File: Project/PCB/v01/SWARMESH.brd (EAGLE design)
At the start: 100 x 80 mm, 45 parts, among them IC1 4051N, M1 MOTOR10MM, M2 MOTOR10MM, Q1 TIP122, U1 ESP32DEVKITC, U3 L293D, U4 7805T

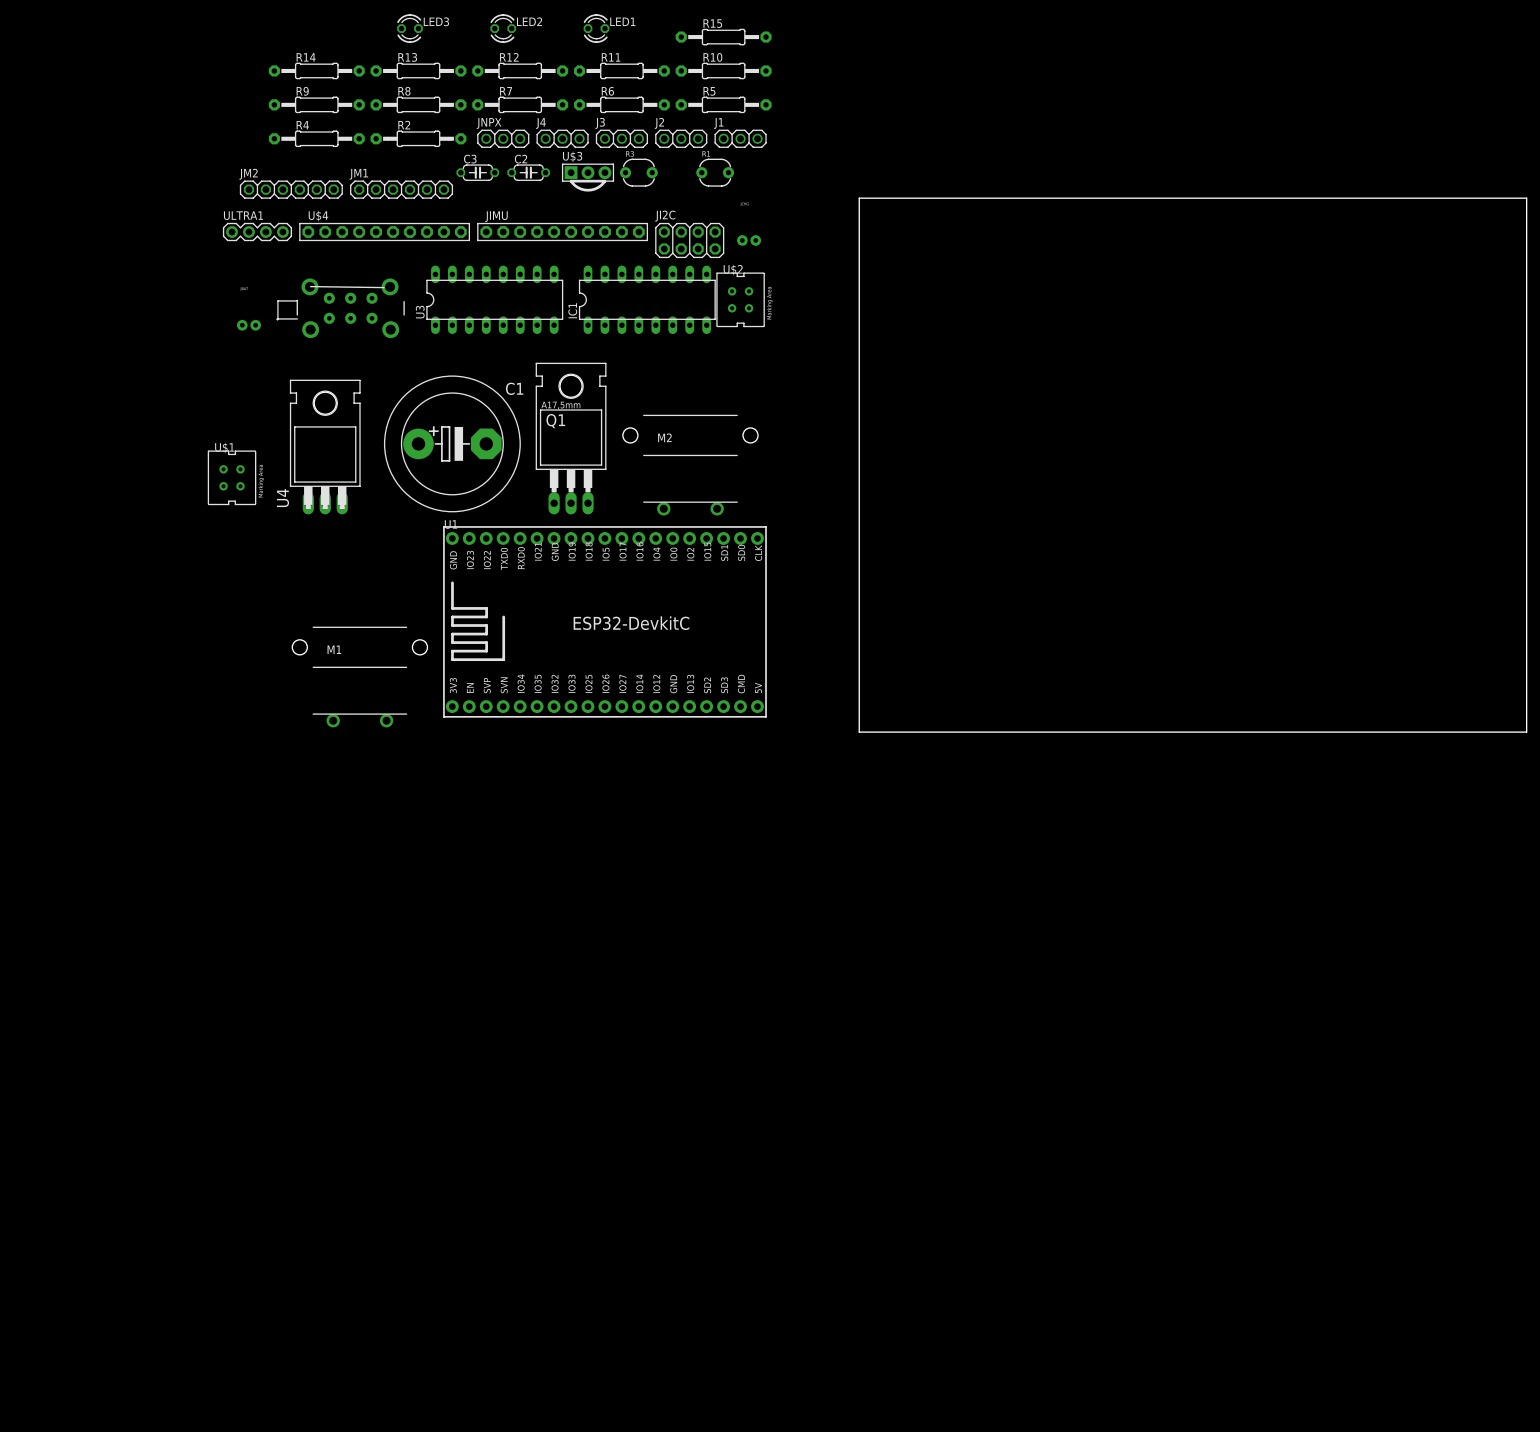
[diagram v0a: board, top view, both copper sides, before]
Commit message: added datasheets
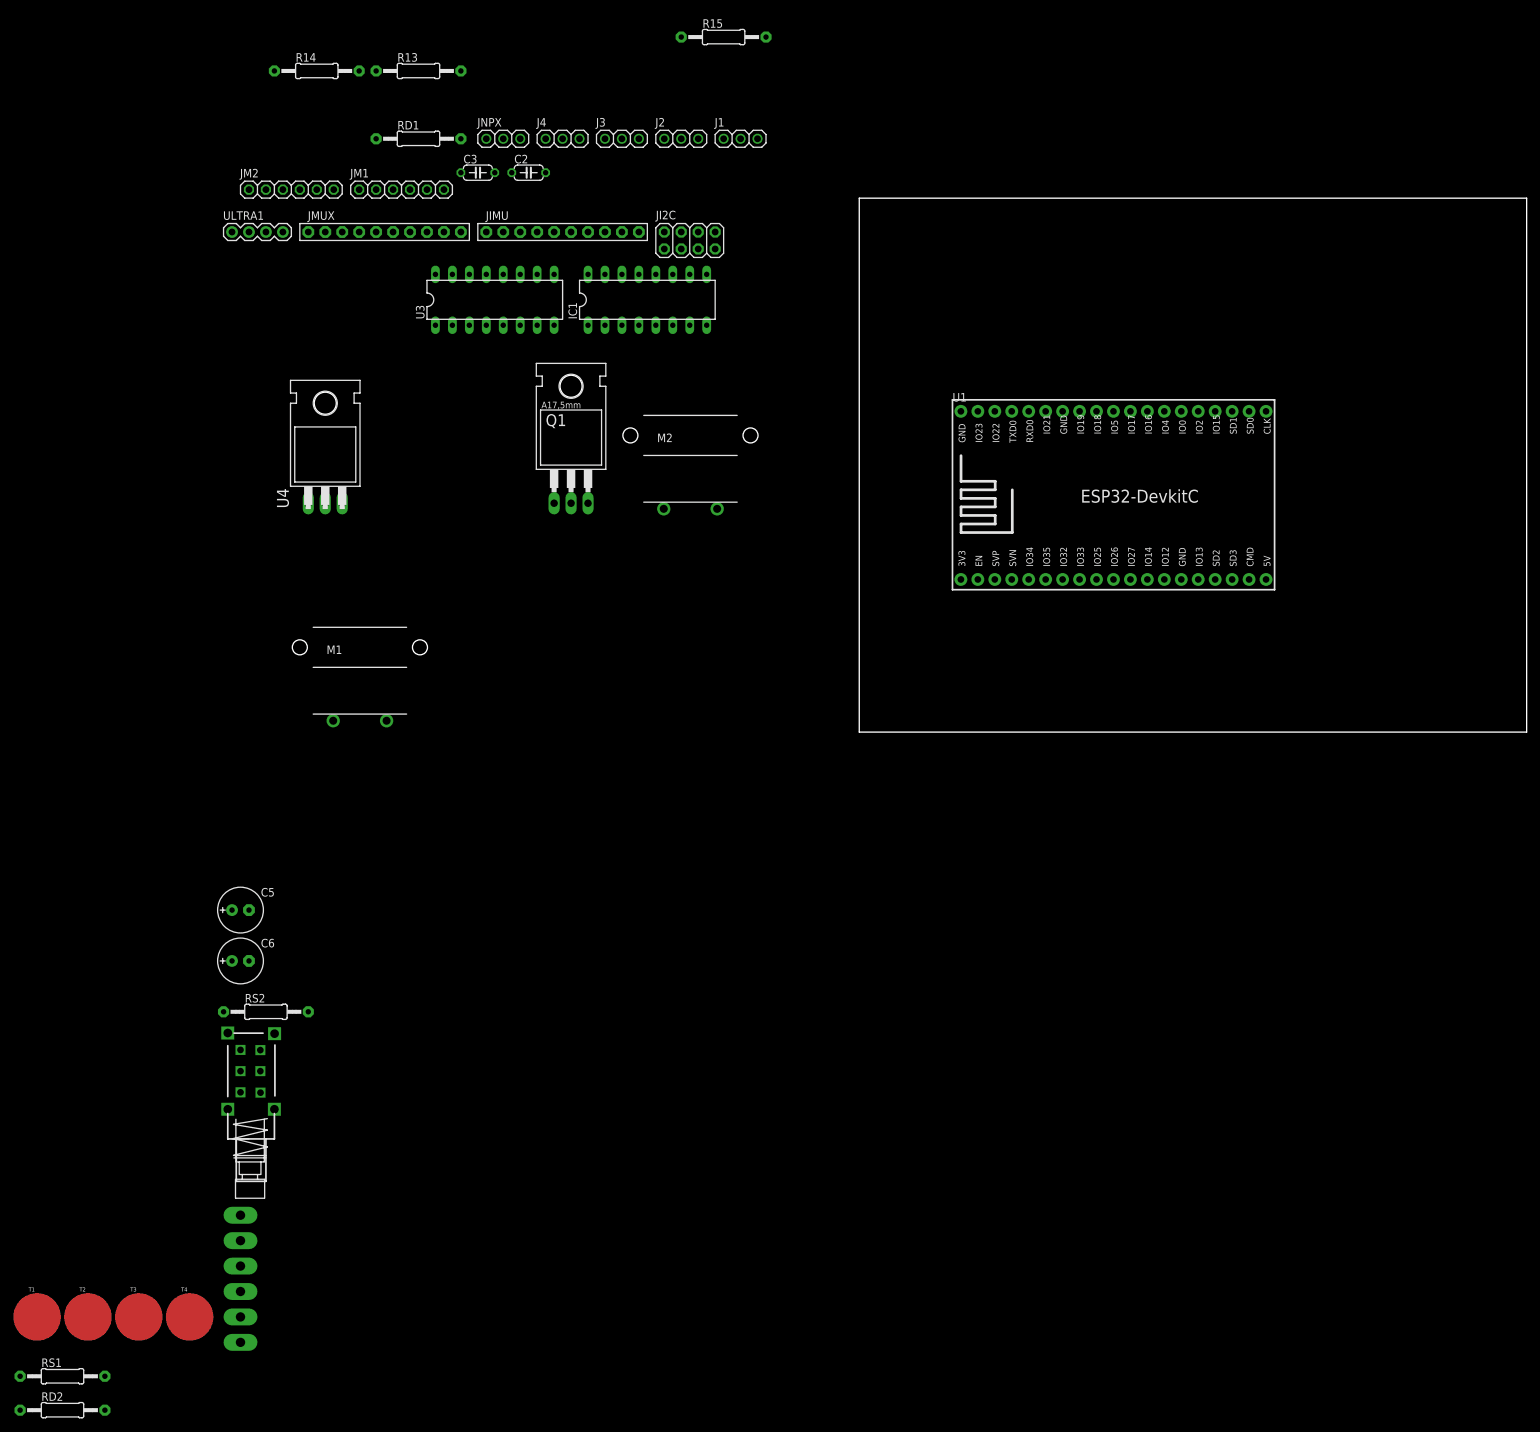
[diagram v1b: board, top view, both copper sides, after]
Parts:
- removed C1: 10uF, adafruit:EB20D
- removed JBAT, JCHG: (no value), SparkFun-Connectors:JST-2-PTH-NS
- removed LED1: TLLG4400, led:LED3MM
- removed LED2: TLLR4400, led:LED3MM
- removed LED3: TLLY4400, led:LED3MM
- removed R1, R3: PHOTOCELLPTH, SparkFun-Sensors:PHOTOCELL
- removed R10, R4, R5, R6, R7: 1k, adafruit:0207/12
- removed R11, R8: 100, adafruit:0207/12
- removed R12, R9: 10k, adafruit:0207/12
- removed S1: (no value), SparkFun-Electromechanical:SWITCHE-DPDT
- removed U$1, U$2: CNY70, cny70:4
- removed U$3: PNA460XM, adafruit:PNA460XM
- added BAT+, BAT-, CHG1+, CHG1-, CHG2+, CHG2-: (no value), adafruit:1X1-BIGPOGO
- added C5, C6: 10uF, adafruit:E2,5-7
- added RD2: 0, adafruit:0207/12
- added RS1, RS2: 150, adafruit:0207/12
- added S2: (no value), ArduinoNano LearningBot 4-21-18:PS22F03
- added T1, T2, T3, T4: (no value), SparkFun-Connectors:SPRING-CONNECTOR
- RD1: value 1k -> 0
- moved U1 78.5 mm to (35.6, 35.6)
- renumbered R2 to RD1, U$4 to JMUX
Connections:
- removed net N$22: R8.1, U$1.A
- removed net N$24: R1.1, R9.2
- removed net N$26: R10.2, U$2.C
- removed net N$35: R12.2, R3.1
- removed net VEE: IC1.7
- new net ADO: JIMU.7
- new net E1A: JM1.3
- new net E1B: JM1.4
- new net E2A: JM2.3
- new net E2B: JM2.4
- new net ECL: JIMU.6
- new net EDA: JIMU.5
- new net FSY: JIMU.10
- new net INT: JIMU.8
- new net M1A: JM1.1, M1.+, U3.3
- new net M1B: JM1.6, M1.-, U3.6
- new net M2A: JM2.1, M2.-, U3.14
- new net M2B: JM2.6, M2.+, U3.11
- new net N$17: JMUX.10, RD1.2, RD2.1
- new net NCS: JIMU.9
- new net SCL: JI2C.5, JI2C.6, JIMU.3, U1.36
- new net SDA: JI2C.7, JI2C.8, JIMU.4, U1.33
- new net TOUCH1: T1.P$2, U1.23
- new net TOUCH2: T2.P$2, U1.24
- new net TOUCH3: T3.P$2, U1.25
- new net TOUCH4: T4.P$2, U1.26
- net GND: now also BAT-.P$1, C3.2, C5.-, C6.-, CHG1-.P$1, CHG2-.P$1, IC1.6, IC1.7, JI2C.3, JI2C.4, JIMU.2, JM1.5, JM2.5, Q1.3, RD2.2; no longer C1.-, JBAT.2, JCHG.2, LED1.K, LED2.K, LED3.K, R1.2, R3.2, U$1.E, U$1.K, U$2.E, U$2.K, U$3.2
- net N$1: now also Q1.1, R13.1; no longer LED1.A, R4.1
- net N$10: now also IC1.12, JMUX.4; no longer M1.+, U3.3
- net N$11: now also IC1.1, JMUX.5; no longer M1.-, U3.6
- net N$12: now also IC1.5, JMUX.6; no longer M2.-, U3.14
- net N$13: now also IC1.2, JMUX.7; no longer M2.+, U3.11
- net N$14: now also IC1.4, JMUX.8; no longer R4.2
- net N$15: now also C3.1, IC1.3; no longer R5.2
- net N$16: now also C6.+, JMUX.9, RS1.1, RS2.1; no longer R6.2
- net N$18: now also IC1.9; no longer R7.2, U$1.C
- net N$19: now also IC1.10; no longer R11.1, U$2.A
- net N$2: now also R13.2; no longer LED2.A, R5.1
- net N$20: now also IC1.11; no longer U$3.1
- net N$21: now also BAT+.P$1, S2.NC1; no longer JCHG.1, S1.2
- net N$3: now also IC1.13, JMUX.1; no longer LED3.A, R6.1
- net N$8: now also IC1.14, JMUX.2; no longer U3.1
- net N$9: now also IC1.15, JMUX.3; no longer U3.9
- net V+: now also C5.+, CHG1+.P$1, CHG2+.P$1, RS2.2, S2.NO1; no longer C1.+, JBAT.1, S1.3
- net VCC: now also JI2C.1, JI2C.2, JIMU.1, JM1.2, JM2.2, RS1.2, U3.1, U3.9; no longer R10.1, R11.2, R12.1, R7.1, R8.2, R9.1, U$3.3

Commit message: added CNY70 & touch sensors
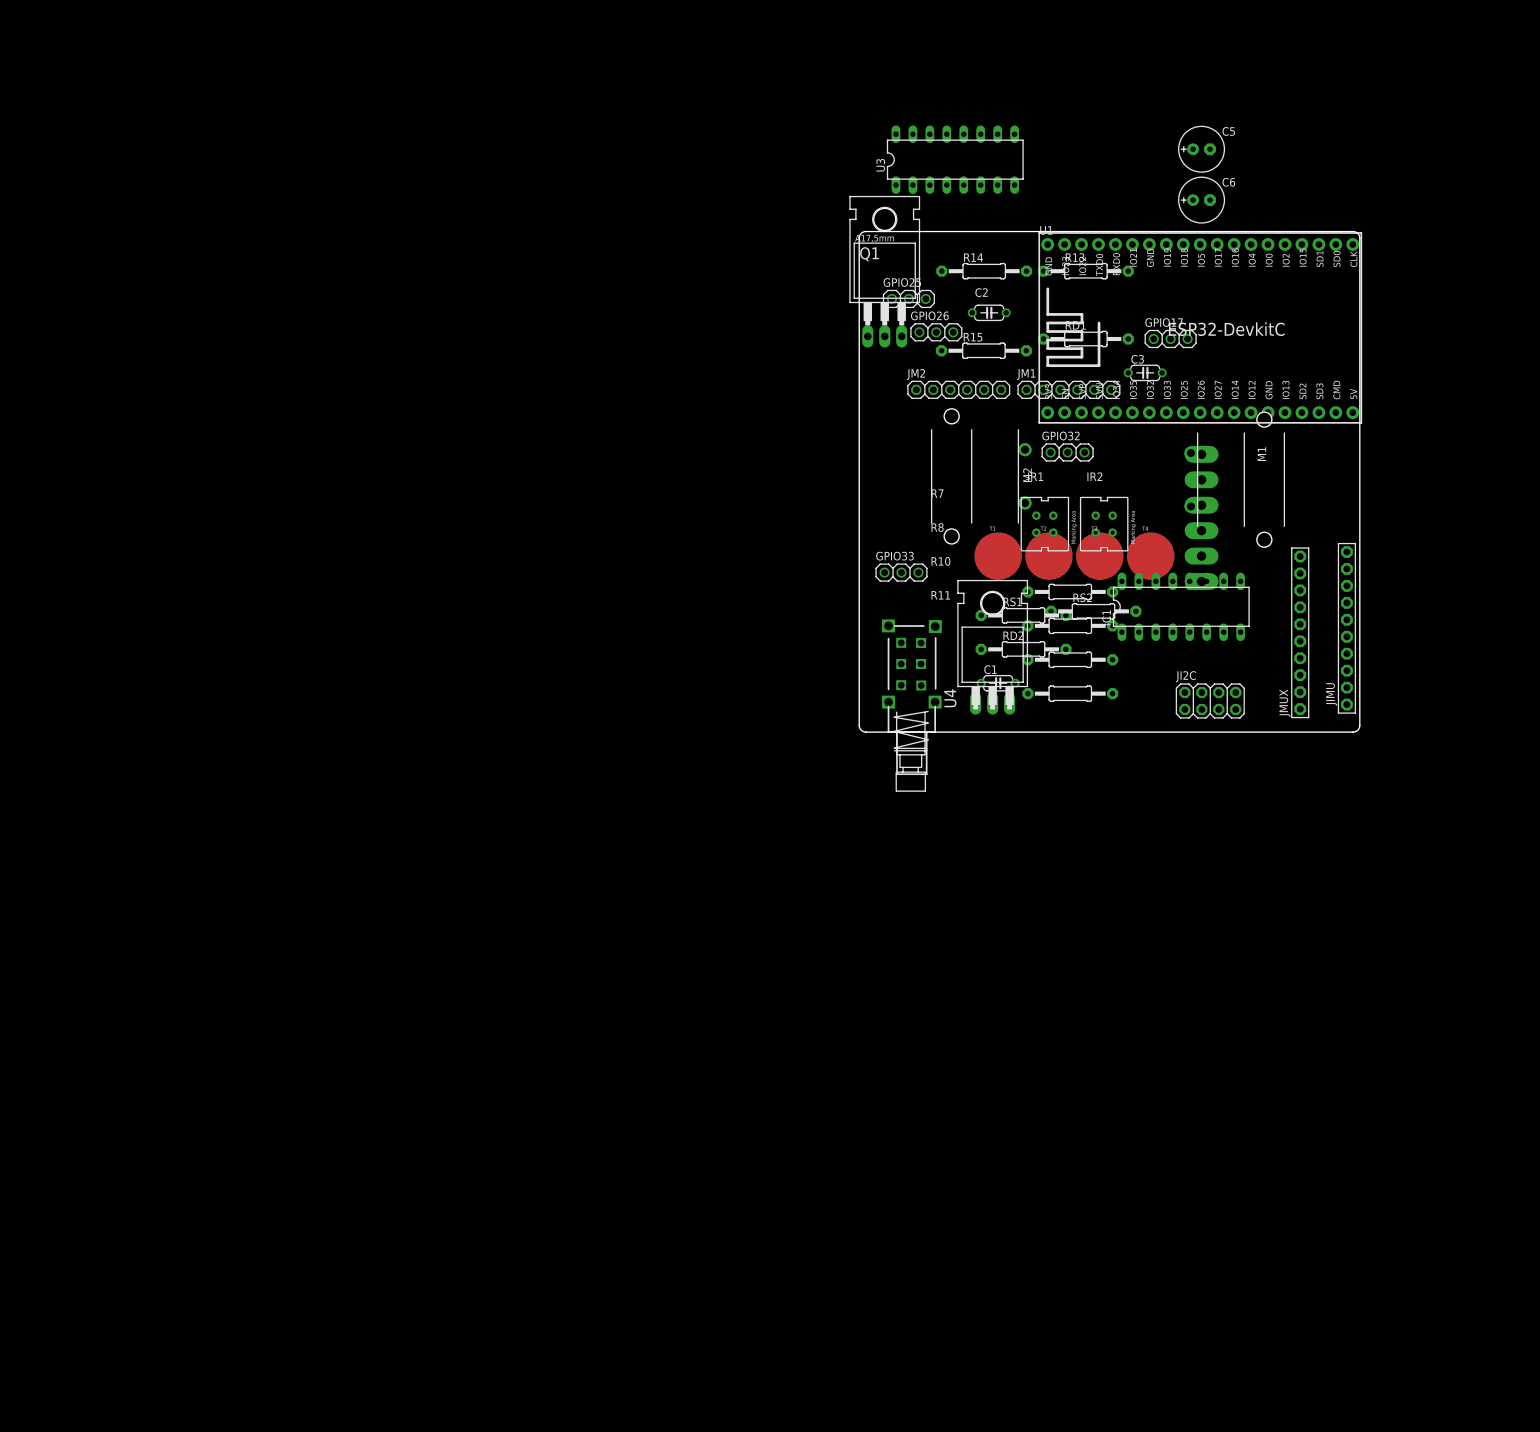
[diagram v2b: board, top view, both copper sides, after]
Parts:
- removed J1, J2, J3, J4, JNPX: (no value), adafruit:1X03
- removed ULTRA1: 1X4-BIG, adafruit:1X04-BIG
- added C1: 0.1uF, adafruit:C050-024X044
- added GPIO17, GPIO25, GPIO26, GPIO32, GPIO33: (no value), adafruit:1X03
- added IR1, IR2: CNY70, cny70:4
- added R10, R7: 1k, adafruit:0207/12
- added R11, R8: 100, adafruit:0207/12
- moved BAT+ 183.7 mm to (51.3, 41.6)
- moved BAT- 183.7 mm to (51.3, 37.8)
- moved C5 183.7 mm to (51.3, 87.3)
- moved C6 183.7 mm to (51.3, 79.7)
- moved CHG1+ 183.7 mm to (51.3, 34.0)
- moved CHG1- 183.7 mm to (51.3, 26.4)
- moved CHG2+ 183.7 mm to (51.3, 30.2)
- moved CHG2- 183.7 mm to (51.3, 22.6)
- moved RD2 183.7 mm to (24.6, 12.4)
- moved RS1 183.7 mm to (24.6, 17.5)
- moved T1 183.7 mm to (20.8, 26.4)
- moved T2 183.7 mm to (28.4, 26.4)
- moved T3 183.7 mm to (36.0, 26.4)
- moved T4 183.7 mm to (43.7, 26.4)
- moved JMUX 149.8 mm to (66.1, 14.9), turned to 90 degrees
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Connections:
- removed net N$15: C3.1, IC1.3
- removed net N$18: IC1.9
- removed net N$2: R13.2
- removed net N$20: IC1.11
- removed net N$23: J1.1
- removed net N$27: ULTRA1.2
- removed net N$28: ULTRA1.3
- removed net N$29: J2.1
- removed net N$30: J3.1
- removed net N$31: J4.1
- removed net N$32: R14.2, R15.1
- removed net N$4: U3.2
- removed net N$5: U3.7
- removed net N$6: U3.15
- removed net N$7: U3.10
- new net ADCMX: C3.1, IC1.3, U1.5
- new net BATLVL: R14.2, R15.1, U1.6
- new net IO18: IC1.10, U1.30
- new net IO19: IC1.9, U1.31
- new net IO25: GPIO25.1, U1.9
- new net IO26: GPIO26.1, U1.10
- new net IO32: GPIO32.1, U1.7
- new net IO33: GPIO33.1, U1.8
- new net IO5: IC1.11, U1.11, U1.12, U1.13, U1.15, U1.29, U3.10, U3.15, U3.2, U3.7
- new net IR1: IR1.C, R7.2, U1.3
- new net IR2: IR2.C, R10.2, U1.4
- new net IRTX: R13.2, U1.37
- new net N$22: IR1.A, R8.1
- net E1A: now also GPIO17.1, U1.28
- net E2A: now also U1.27
- net GND: now also C1.2, GPIO17.3, GPIO25.3, GPIO26.3, GPIO32.3, GPIO33.3, IR1.E, IR1.K, IR2.E, IR2.K, U1.14; no longer J1.3, J2.3, J3.3, J4.3, ULTRA1.4
- net N$19: now also IR2.A, R11.1; no longer IC1.10
- net VCC: now also C1.1, GPIO17.2, GPIO25.2, GPIO26.2, GPIO32.2, GPIO33.2, R10.1, R11.2, R7.1, R8.2; no longer J1.2, J2.2, J3.2, J4.2, ULTRA1.1
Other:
- board size 100 x 80 mm -> 75 x 75 mm

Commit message: first revision
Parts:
- moved JMUX 76.3 mm to (41.1, 87.0)
- moved C6 75.8 mm to (3.03, 21.3)
- moved JIMU 75.8 mm to (44.7, 85.8), turned to 270 degrees
- moved T1 63.0 mm to (62.8, 73.4)
- moved T2 50.4 mm to (39.5, 75.5)
- moved T4 47.8 mm to (54.2, 73.0)
- moved T3 47.5 mm to (45.6, 73.0)
- moved IR2 45.7 mm to (71.9, 2.00)
- moved GPIO33 41.0 mm to (26.6, 59.5)
- moved IR1 36.9 mm to (3.73, 3.22)
- moved IC1 36.6 mm to (44.8, 55.2), turned to 180 degrees
- moved S2 33.0 mm to (7.66, 43.2), turned to 270 degrees
- moved U3 30.6 mm to (34.7, 62.9)
- moved U1 26.0 mm to (49.6, 34.6)
- moved M2 26.0 mm to (3.85, 53.3)
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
